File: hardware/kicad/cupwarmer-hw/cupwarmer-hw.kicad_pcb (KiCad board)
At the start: 4 copper layers, 56 x 56 mm, 48 parts, among them J1 I2C Service, J2 THERM_MON, J3 STATUS_MON, Q1 AO3400 SOT-23, U1 STWLC38JRM

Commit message: Set STWLC38 NTC pull-up to 51k
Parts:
- R7: value 10k -> 51k
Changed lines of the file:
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@@
 			)
 		)
-		(property "Value" "10k"
+		(property "Value" "51k"
 			(at 0 1.43 0)
 			(layer "F.Fab")

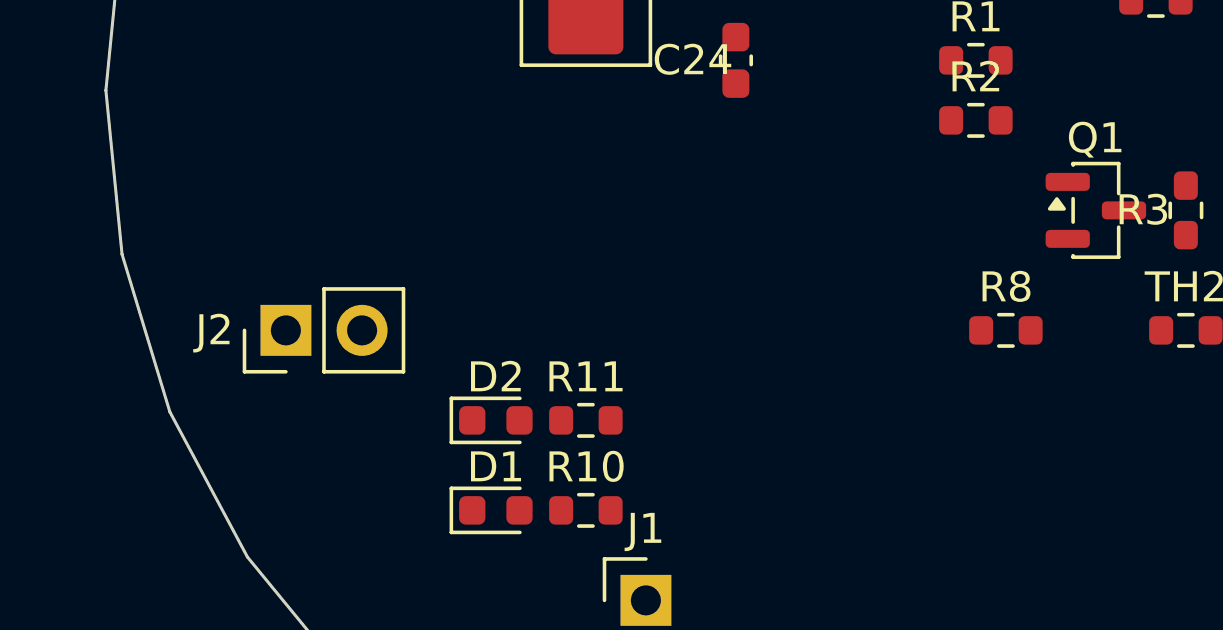
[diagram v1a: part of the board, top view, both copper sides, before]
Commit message: Sync PCB values and remove unused monitor footprints
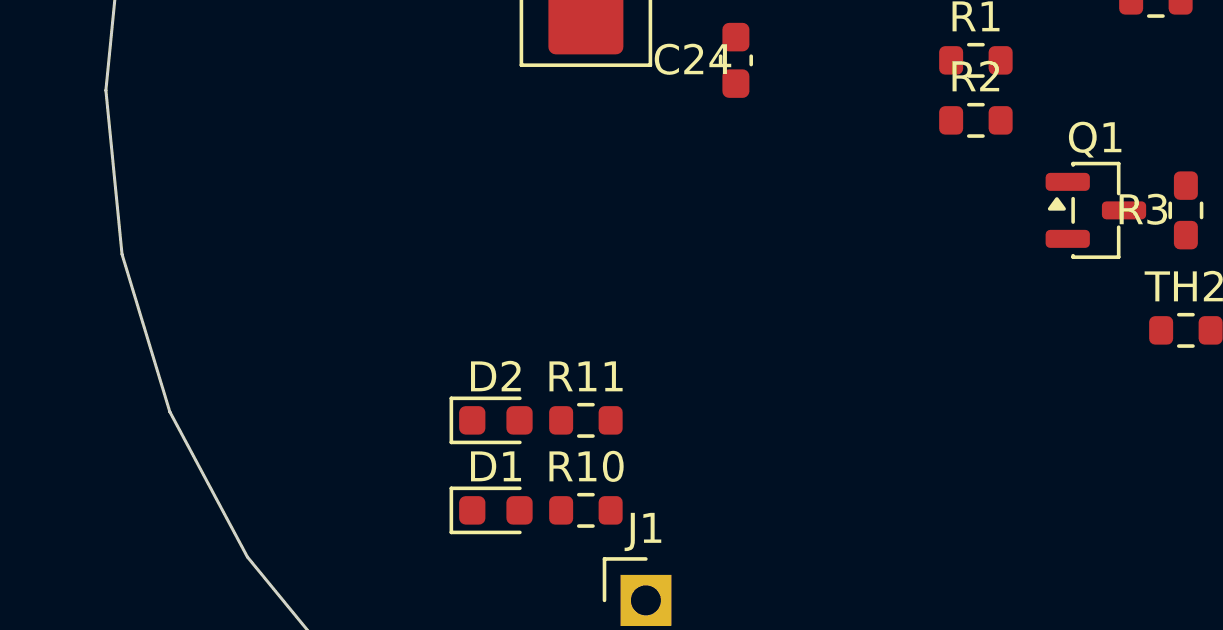
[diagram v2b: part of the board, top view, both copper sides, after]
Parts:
- removed J2: THERM_MON, Connector_PinHeader_2.54mm:PinHeader_1x02_P2.54mm_Vertical
- removed R8: 10k Pull-up, Resistor_SMD:R_0603_1608Metric
- C18, C19: value 100nF -> 10nF
- C2, C20, C21, C23: value 10uF/25V -> 10uF/35V
- C9: value 10uF -> 10uF/35V

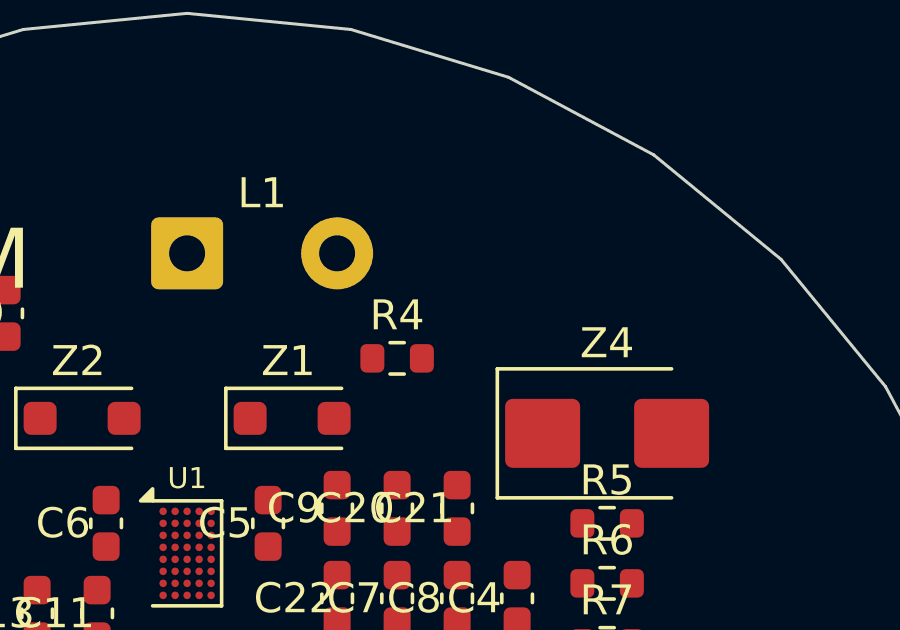
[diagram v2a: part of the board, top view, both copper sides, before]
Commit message: Add parallel SOVP clamp resistors
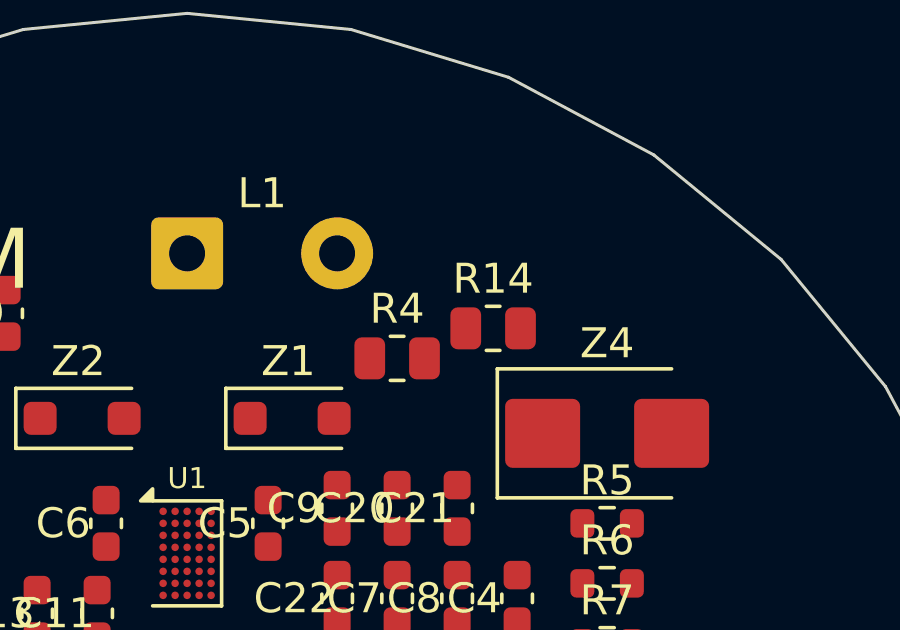
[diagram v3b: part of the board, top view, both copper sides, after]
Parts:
- added R14: RCL 200R, Resistor_SMD:R_0805_2012Metric, F.Cu at (110.2, 82.5)
- R4: value RCL 300R -> RCL 200R; footprint Resistor_SMD:R_0603_1608Metric -> Resistor_SMD:R_0805_2012Metric
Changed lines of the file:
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@@
 		)
 	)
-	(footprint "Resistor_SMD:R_0603_1608Metric"
+	(footprint "Resistor_SMD:R_0805_2012Metric"
 		(layer "F.Cu")
 		(at 107 83.5 0)
-		(descr "Resistor SMD 0603 (1608 Metric), square (rectangular) end terminal, IPC-7351 nominal, (Body size source: IPC-SM-782 page 72, https://www.pcb-3d.com/wordpress/wp-content/uploads/ipc-sm-782a_amendment_1_and_2.pdf)")
+		(descr "Resistor SMD 0805 (2012 Metric), square (rectangular) end terminal, IPC-7351 nominal, (Body size source: IPC-SM-782 page 72, https://www.pcb-3d.com/wordpress/wp-content/uploads/ipc-sm-782a_amendment_1_and_2.pdf)")
 		(tags "resistor")
 		(property "Reference" "R4"
-			(at 0 -1.43 0)
+			(at 0 -1.65 0)
 			(layer "F.SilkS")
 			(effects
@@
 			)
 		)
-		(property "Value" "RCL 300R"
-			(at 0 1.43 0)
+		(property "Value" "RCL 200R"
+			(at 0 1.65 0)
 			(layer "F.Fab")
 			(effects
@@
 		(duplicate_pad_numbers_are_jumpers no)
 		(fp_line
-			(start -0.237258 -0.5225)
-			(end 0.237258 -0.5225)
+			(start -0.227064 -0.735)
+			(end 0.227064 -0.735)
 			(stroke
 				(width 0.12)
@@
 		)
 		(fp_line
-			(start -0.237258 0.5225)
-			(end 0.237258 0.5225)
+			(start -0.227064 0.735)
+			(end 0.227064 0.735)
 			(stroke
 				(width 0.12)
@@
 		)
 		(fp_rect
-			(start -1.48 -0.73)
-			(end 1.48 0.73)
+			(start -1.68 -0.95)
+			(end 1.68 0.95)
 			(stroke
 				(width 0.05)
@@
 		)
 		(fp_rect
-			(start -0.8 -0.4125)
-			(end 0.8 0.4125)
+			(start -1 -0.625)
+			(end 1 0.625)
 			(stroke
 				(width 0.1)
@@
 			(effects
 				(font
-					(size 0.4 0.4)
-					(thickness 0.06)
+						(size 0.5 0.5)
+						(thickness 0.08)
 				)
 			)
 		)
 		(pad "1" smd roundrect
-			(at -0.825 0)
-			(size 0.8 0.95)
+			(at -0.9125 0)
+			(size 1.025 1.4)
 			(layers "F.Cu" "F.Mask" "F.Paste")
-			(roundrect_rratio 0.25)
+			(roundrect_rratio 0.243902)
 		)
 		(pad "2" smd roundrect
-			(at 0.825 0)
-			(size 0.8 0.95)
+			(at 0.9125 0)
+			(size 1.025 1.4)
 			(layers "F.Cu" "F.Mask" "F.Paste")
-			(roundrect_rratio 0.25)
+			(roundrect_rratio 0.243902)
 		)
 		(embedded_fonts no)
-		(model "${KICAD10_3DMODEL_DIR}/Resistor_SMD.3dshapes/R_0603_1608Metric.step"
+		(model "${KICAD10_3DMODEL_DIR}/Resistor_SMD.3dshapes/R_0805_2012Metric.step"
 			(offset
 				(xyz 0 0 0)
@@
 			(offset
 				(xyz 0 0 0)
+			)
+			(scale
+				(xyz 1 1 1)
+			)
+			(rotate
+				(xyz 0 0 0)
+			)
+		)
+	)
+	(footprint "Resistor_SMD:R_0805_2012Metric"
+		(layer "F.Cu")
+		(at 110.2 82.5 0)
+		(descr "Resistor SMD 0805 (2012 Metric), square (rectangular) end terminal, IPC-7351 nominal, (Body size source: IPC-SM-782 page 72, https://www.pcb-3d.com/wordpress/wp-content/uploads/ipc-sm-782a_amendment_1_and_2.pdf)")
+		(tags "resistor")
+		(property "Reference" "R14"
+			(at 0 -1.65 0)
+			(layer "F.SilkS")
+			(effects
+				(font
+					(size 1 1)
+					(thickness 0.15)
+				)
+			)
+		)
+		(property "Value" "RCL 200R"
+			(at 0 1.65 0)
+			(layer "F.Fab")
+			(effects
+				(font
+					(size 1 1)
+					(thickness 0.15)
+				)
+			)
+		)
+		(property "KiLib_Generator" "SMD_2terminal_chip_molded"
+			(at 0 0 0)
+			(layer "F.SilkS")
+			(hide yes)
+			(effects
+				(font
+					(size 1 1)
+					(thickness 0.15)
+				)
+			)
+		)
+		(attr smd)
+		(duplicate_pad_numbers_are_jumpers no)
+		(fp_line
+			(start -0.227064 -0.735)
+			(end 0.227064 -0.735)
+			(stroke
+				(width 0.12)
+				(type solid)
+			)
+			(layer "F.SilkS")
+		)
+		(fp_line
+			(start -0.227064 0.735)
+			(end 0.227064 0.735)
+			(stroke
+				(width 0.12)
+				(type solid)
+			)
+			(layer "F.SilkS")
+		)
+		(fp_rect
+			(start -1.68 -0.95)
+			(end 1.68 0.95)
+			(stroke
+				(width 0.05)
+				(type solid)
+			)
+			(fill no)
+			(layer "F.CrtYd")
+		)
+		(fp_rect
+			(start -1 -0.625)
+			(end 1 0.625)
+			(stroke
+				(width 0.1)
+				(type solid)
+			)
+			(fill no)
+			(layer "F.Fab")
+		)
+		(fp_text user "${REFERENCE}"
+			(at 0 0 0)
+			(layer "F.Fab")
+			(effects
+				(font
+					(size 0.5 0.5)
+					(thickness 0.08)
+				)
+			)
+		)
+		(pad "1" smd roundrect
+			(at -0.9125 0)
+			(size 1.025 1.4)
+			(layers "F.Cu" "F.Mask" "F.Paste")
+			(roundrect_rratio 0.243902)
+		)
+		(pad "2" smd roundrect
+			(at 0.9125 0)
+			(size 1.025 1.4)
+			(layers "F.Cu" "F.Mask" "F.Paste")
+			(roundrect_rratio 0.243902)
+		)
+		(embedded_fonts no)
+		(model "${KICAD10_3DMODEL_DIR}/Resistor_SMD.3dshapes/R_0805_2012Metric.step"
+			(offset
+				(xyz 0 0 0)

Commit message: Change power indicator LED to red
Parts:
- D1: value LED Green -> LED Red
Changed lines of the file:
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@@
 			)
 		)
-		(property "Value" "LED Green"
+		(property "Value" "LED Red"
 			(at 0 1.43 0)
 			(layer "F.Fab")
